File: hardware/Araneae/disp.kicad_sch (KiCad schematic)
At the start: 1 part, among them J2 FH12-22S-0.5SH55

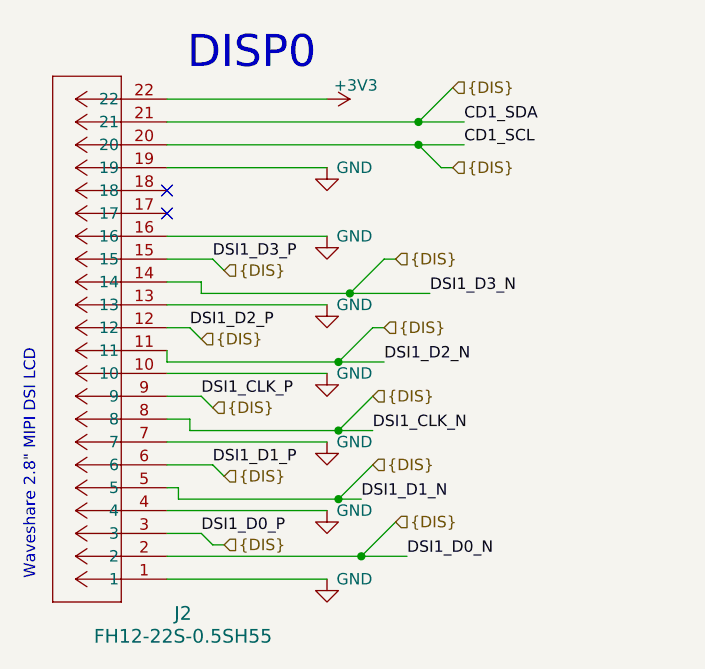
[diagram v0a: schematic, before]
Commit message: Add CI workflow for PCB checks and artifact generation
- Created a GitHub Actions workflow (`ci.yml`) to automate hardware checks including ERC, DRC, and plot generation for KiCad projects.
- Added a new footprint for the SON50P200X200X80-9N component in `SON50P200X200X80-9N.kicad_mod`.
- Introduced a new symbol for the TPS22965DSGR component in `TPS22965DSGR.kicad_sym`.
- Added a configuration file `kibot.yaml` for generating fabrication files and other outputs.
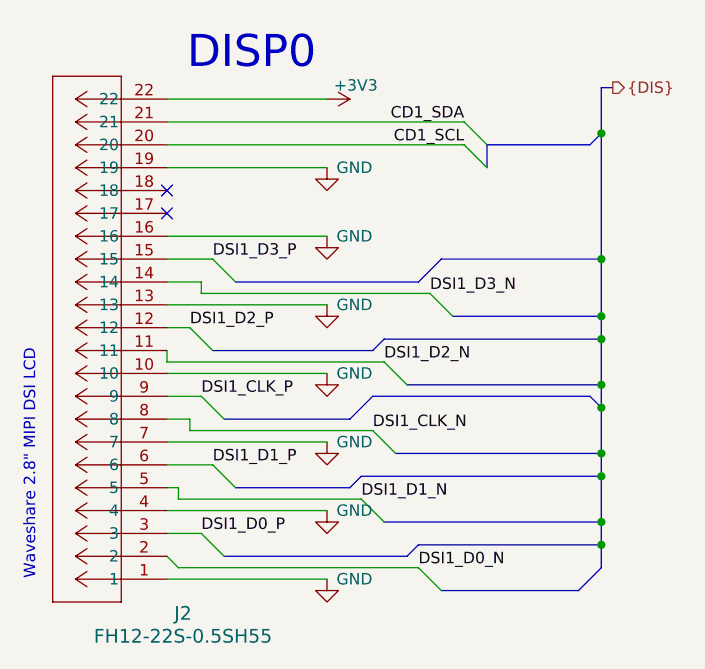
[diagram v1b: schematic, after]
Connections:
- net {DIS}: no longer J2.11, J2.12, J2.14, J2.15, J2.2, J2.20, J2.21, J2.3, J2.5, J2.6, J2.8, J2.9
- new net CD1_SCL: J2.20
- new net CD1_SDA: J2.21
- new net DSI1_CLK_N: J2.8
- new net DSI1_CLK_P: J2.9
- new net DSI1_D0_N: J2.2
- new net DSI1_D0_P: J2.3
- new net DSI1_D1_N: J2.5
- new net DSI1_D1_P: J2.6
- new net DSI1_D2_N: J2.11
- new net DSI1_D2_P: J2.12
- new net DSI1_D3_N: J2.14
- new net DSI1_D3_P: J2.15
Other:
- company: (none) -> Matheus Henrique(Aka: TheusHen)
- title: (none) -> Araneae
